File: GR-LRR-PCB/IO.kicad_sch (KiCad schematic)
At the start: 0 parts

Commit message: starting first layout
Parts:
- added D1: BAT20JFILM, Diode_SMD:D_SOD-323_HandSoldering, symbol Device:D
- added D2: QTLP650C2TR, Diode_SMD:D_1206_3216Metric_Pad1.42x1.75mm_HandSolder, symbol Device:LED
- added IC2: MC1413DR2G, SOIC127P600X175-16N, symbol MC1413DR2G:MC1413DR2G
- added J10: Limit Switch, Connector_PinHeader_2.54mm:PinHeader_1x03_P2.54mm_Vertical, symbol Connector:Conn_01x03_Pin
- added J13: UT Sensor, Connector_PinHeader_2.54mm:PinHeader_1x05_P2.54mm_Vertical, symbol Connector:Conn_01x05_Pin
- added J5: StepperDriver1, Connector_PinHeader_2.54mm:PinHeader_1x08_P2.54mm_Vertical, symbol Connector:Conn_01x08_Pin
- added J6: StepperDriver2, Connector_PinHeader_2.54mm:PinHeader_1x08_P2.54mm_Vertical, symbol Connector:Conn_01x08_Pin
- added J7: StepperDriver3, Connector_PinHeader_2.54mm:PinHeader_1x08_P2.54mm_Vertical, symbol Connector:Conn_01x08_Pin
- added J8: StepperDriver4, Connector_PinHeader_2.54mm:PinHeader_1x08_P2.54mm_Vertical, symbol Connector:Conn_01x08_Pin
- added J9: STATE LED, Connector_PinHeader_2.54mm:PinHeader_1x04_P2.54mm_Vertical, symbol Connector:Conn_01x04_Pin
- added K1: G5LE-14-DC5, G5LE-14_SPDT, symbol G5LE-14-DC5:G5LE-14-DC5
- added Q1, Q2: BSS806NH6327XTSA1, BSS806NH6327XTSA1:BSS806NH6327XTSA1, symbol BSS806NH6327XTSA1:BSS806NH6327XTSA1
- added R1, R10, R11, R13, R14, R15, R16, R17, R18, R19, R2, R20, R21, R3, R5, R6, R7, R8: R, Resistor_SMD:R_1206_3216Metric_Pad1.30x1.75mm_HandSolder, symbol Device:R
- added R12: 150ohm, 0.05w, min, Resistor_SMD:R_1206_3216Metric_Pad1.30x1.75mm_HandSolder, symbol Device:R
- added R4: 10k, Resistor_SMD:R_1206_3216Metric_Pad1.30x1.75mm_HandSolder, symbol Device:R
- added SW1: XA1E-BV302-R, XA1E-BV302-R:XA1E-BV302-R, symbol XA1E-BV302-R:XA1E-BV302-R
- added StepperMotor1: StepperMotor1, Connector_PinHeader_2.54mm:PinHeader_1x04_P2.54mm_Vertical, symbol Connector:Conn_01x04_Pin
- added StepperMotor2: StepperMotor2, Connector_PinHeader_2.54mm:PinHeader_1x04_P2.54mm_Vertical, symbol Connector:Conn_01x04_Pin
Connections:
- new net: D1.2 (A), D2.1 (K), K1.2 (COIL_1), Q1.3 (D)
- new net: D2.2 (A), R12.1
- new net: J13.3 (Pin_3), R10.1
- new net: J13.5 (Pin_5), Q2.3 (D), R13.2, R14.1
- new net: J10.3 (Pin_3), R5.1
- new net: J10.1 (Pin_1), R4.2
- new net: IC2.16 (OUT_7), R6.1
- new net: J9.2 (Pin_2), R6.2
- new net: J9.3 (Pin_3), R7.2
- new net: J9.4 (Pin_4), R8.2
- new net: K1.1 (COM), SW1.1, SW1.3
- new net: IC2.15 (OUT_6), R7.1
- new net: IC2.14 (OUT_5), R8.1
- new net +24V: J13.2 (Pin_2), J13.4 (Pin_4), J9.1 (Pin_1), K1.3 (NO)
- new net +3.3V: R13.1
- new net +5V: D1.1 (K), J6.7 (Pin_7), J8.7 (Pin_7), K1.5 (COIL_2), R1.1, R12.2, R18.1, R20.1, R3.1, R4.1
- new net ANALOG_A0: R10.2, R11.1
- new net ANALOG_A1: R15.2, R16.1
- new net BATT_VIN: R15.1
- new net DIR1: J5.1 (Pin_1)
- new net DIR2: J7.1 (Pin_1)
- new net EN1: J5.8 (Pin_8), J7.8 (Pin_8), R1.2, R2.1
- new net GND: IC2.8 (GND), J13.1 (Pin_1), J6.2 (Pin_2), J6.8 (Pin_8), J8.2 (Pin_2), J8.8 (Pin_8), Q1.2 (S), Q2.2 (S), R11.2, R14.2, R16.2, R17.2, R19.2, R2.2, R21.2, R5.2
- new net GPIO_2: Q1.1 (G)
- new net GPIO_5: J10.2 (Pin_2)
- new net GPIO_6: Q2.1 (G)
- new net MS1_1: J5.7 (Pin_7), J7.7 (Pin_7), R17.1, R3.2
- new net MS2_1: J5.6 (Pin_6), J7.6 (Pin_6), R18.2, R19.1
- new net OA1_1: J6.4 (Pin_4), StepperMotor1.3 (Pin_3)
- new net OA1_2: J8.4 (Pin_4), StepperMotor2.2 (Pin_2)
- new net OA2_1: J6.3 (Pin_3), StepperMotor1.4 (Pin_4)
- new net OA2_2: J8.3 (Pin_3), StepperMotor2.1 (Pin_1)
- new net OB1_1: J6.5 (Pin_5), StepperMotor1.2 (Pin_2)
- new net OB1_2: J8.5 (Pin_5), StepperMotor2.3 (Pin_3)
- new net OB2_1: J6.6 (Pin_6), StepperMotor1.1 (Pin_1)
- new net OB2_2: J8.6 (Pin_6), StepperMotor2.4 (Pin_4)
- new net PWM_0: J5.2 (Pin_2)
- new net PWM_1: J7.2 (Pin_2)
- new net SPREAD1: J5.5 (Pin_5), J7.5 (Pin_5), R20.2, R21.1
- new net VM: J6.1 (Pin_1), J8.1 (Pin_1), SW1.2, SW1.4
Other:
- note added: "1 BLUE - GND 2. BROWN - 24V 3. WHITE - OUTPUT - 0 to 10V 4. BLACK - 24V - Sets Fast Read Mode 5. GREY - Teach"
- note added: "1. Motor Drivers 2. H7 Mount 3. 24v to 5v 4. 5v to 3.3v 5. UT 6. Motor Wire mount 7. Relay mount 8. clamp sensor 9. encoder 10. linear transducer 11. Hard estop 12. main battery power in 13. Battery Monitor"
- note added: "LED Driver"
- note added: "Stepper drivers TMC2209 SlicentStepSticks"
- note added: "This voltage divider needs to be adjusted so that the teach pin is given 2 volts"
- note added: "This voltage divider needs to be adjusted to measure the battery voltage"
- note added: "This voltage divider needs to scale the 0 to 10v output of the sensor to the analog input range of the device"
- note added: "VCC RED YELLOW GREEN"

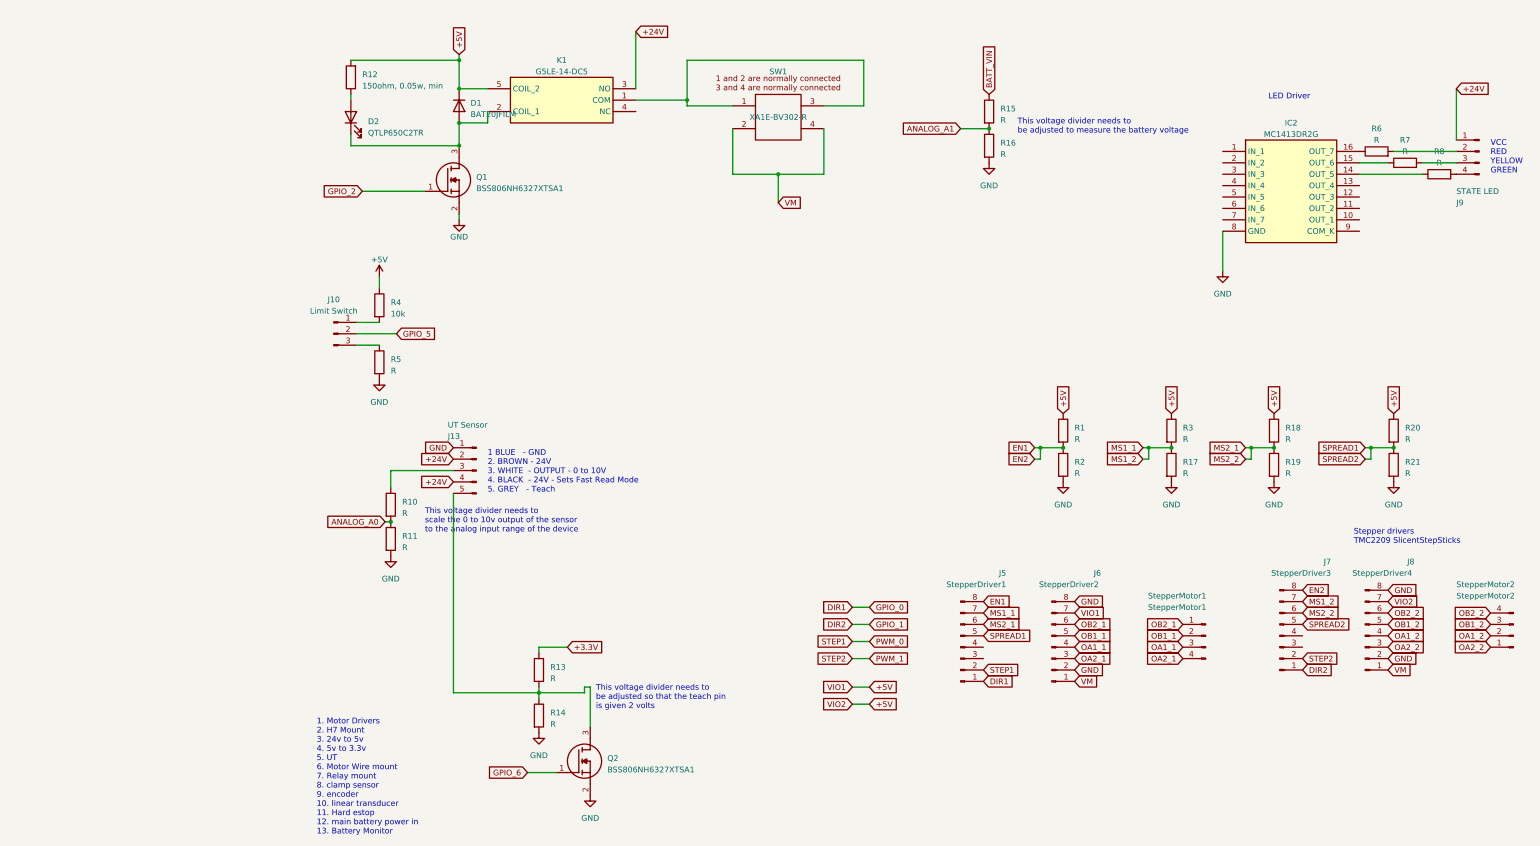
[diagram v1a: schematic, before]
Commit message: new smaller layout
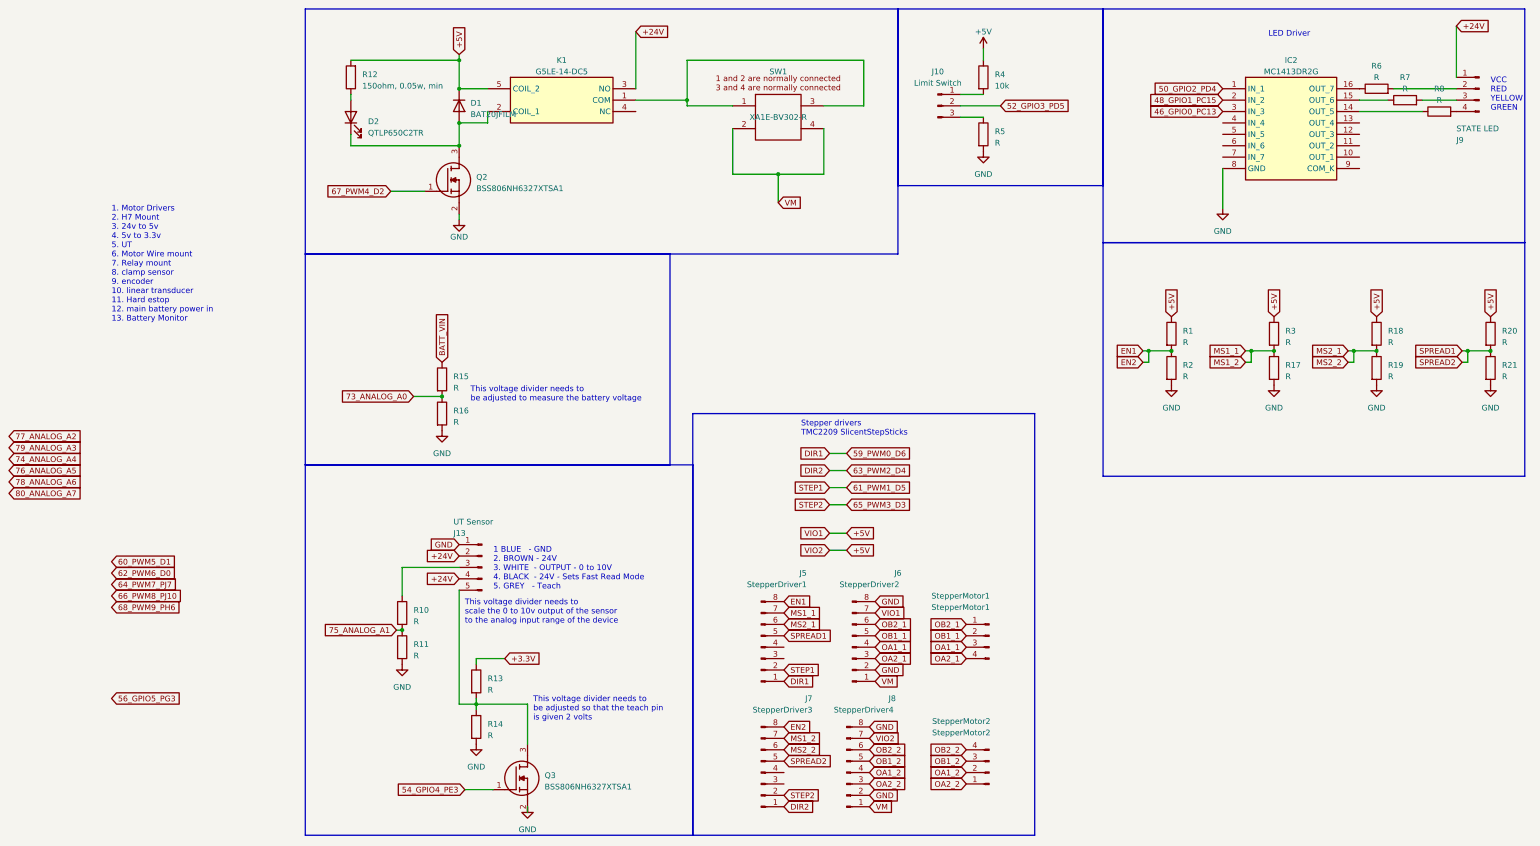
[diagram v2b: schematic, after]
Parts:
- Q2: renamed from Q1; footprint BSS806NH6327XTSA1:BSS806NH6327XTSA1 -> BSS806NH6327XTSA1:SOT95P240X110-3N
- Q3: renamed from Q2; footprint BSS806NH6327XTSA1:BSS806NH6327XTSA1 -> BSS806NH6327XTSA1:SOT95P240X110-3N
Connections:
- net 50_GPIO2_PD4: now reaches IC2.1 (IN_1)
- net 48_GPIO1_PC15: now reaches IC2.2 (IN_2)
- net 46_GPIO0_PC13: now reaches IC2.3 (IN_3)
- net ANALOG_A0 renamed 75_ANALOG_A1
- net ANALOG_A1 renamed 73_ANALOG_A0
- net DIR1 renamed 59_PWM0_D6
- net DIR2 renamed 63_PWM2_D4
- net GPIO_2 renamed 67_PWM4_D2
- net GPIO_5 renamed 52_GPIO3_PD5
- net GPIO_6 renamed 54_GPIO4_PE3
- net PWM_0 renamed 61_PWM1_D5
- net PWM_1 renamed 65_PWM3_D3
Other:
- moved on the sheet: IC2, J10, J13, J5, J6, J7, J8, J9, Q3, R1, R10, R11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
